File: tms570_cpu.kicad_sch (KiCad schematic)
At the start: 53 parts, among them J12 TSW-103-08-F-S-RA, J3 FTSH-105-01-L-DV-K, U2 TMS570LS0914APGEQQ1

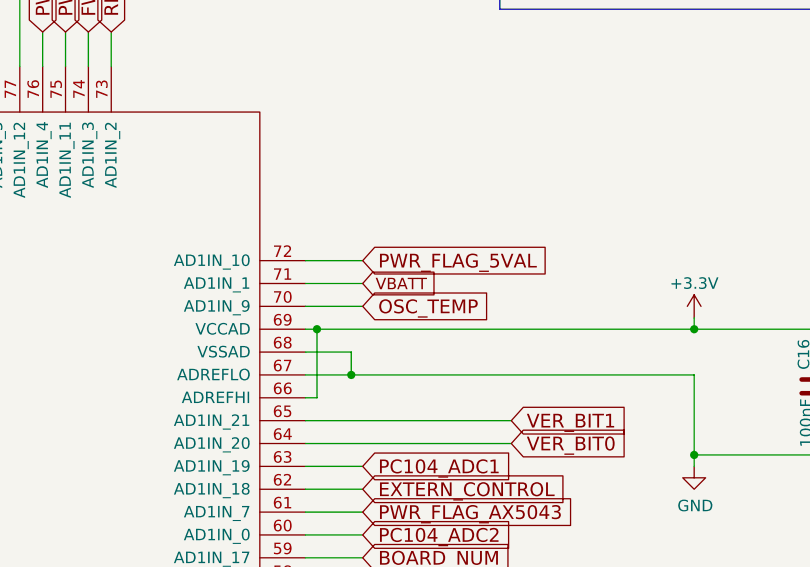
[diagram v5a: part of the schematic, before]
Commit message: Run some more GPIOs from the antenna controller to the PC104
Just for good measure.  Also rename VBATT to VBAT to match the power
supply name.

Signed-off-by: Corey Minyard <corey@minyard.net>
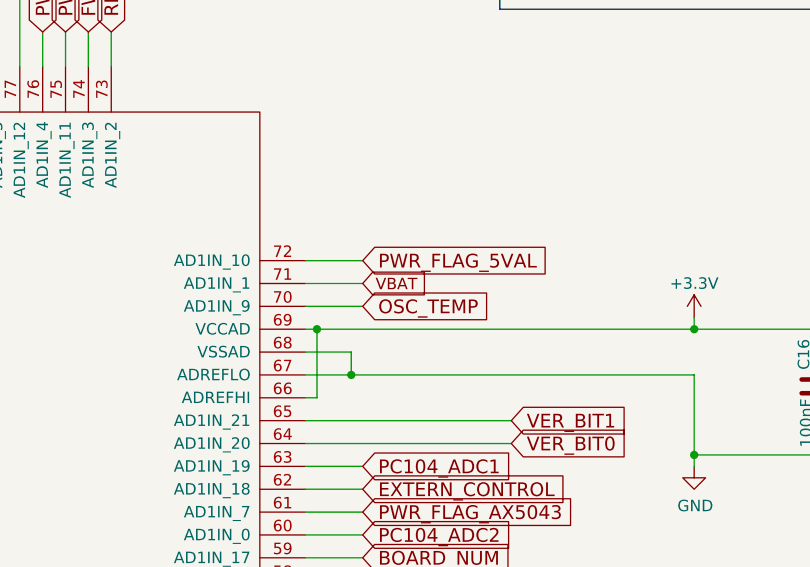
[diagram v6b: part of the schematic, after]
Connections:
- net VBATT renamed VBAT
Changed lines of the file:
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@@
 		)
 	)
-	(global_label "VBATT"
+	(global_label "VBAT"
 		(shape input)
 		(at 288.29 96.52 0)

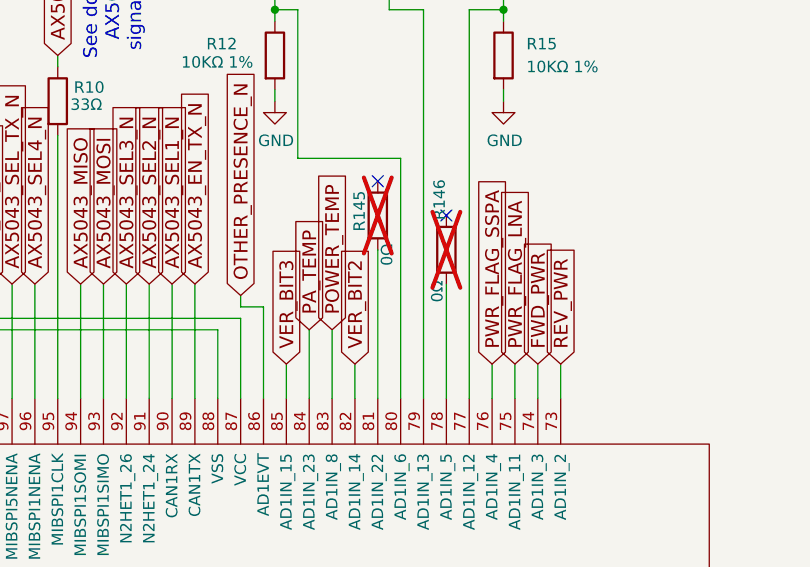
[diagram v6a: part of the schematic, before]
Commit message: Do some work on PC104 ADC/GPIO
Run the last two ADC lines from the TMS570 to the PC104.  Document this
and document how the PC104 lines from the antenna controller may be
used.

Signed-off-by: Corey Minyard <corey@minyard.net>
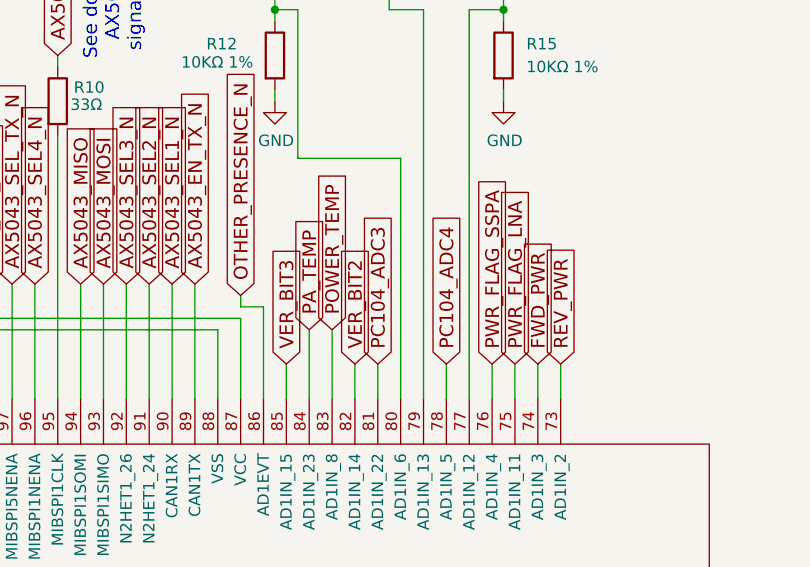
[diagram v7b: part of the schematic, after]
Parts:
- removed R145, R146: 0Ω, Resistor_SMD:R_0402_1005Metric_Pad0.72x0.64mm_HandSolder, symbol Device:R
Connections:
- net PC104_ADC4: now reaches U2.78 (AD1IN_5)
- net PC104_ADC3: now reaches U2.81 (AD1IN_22)
- no-connect marks 4 -> 2
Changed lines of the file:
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@@
 	)
 	(no_connect
-		(at 247.65 52.07)
-	)
-	(no_connect
 		(at 217.17 204.47)
 	)
-	(no_connect
-		(at 240.03 48.26)
-	)
 	(wire
 		(pts
@@
 	(wire
 		(pts
-			(xy 247.65 59.69) (xy 247.65 72.39)
+			(xy 247.65 68.58) (xy 247.65 72.39)
 		)
 		(stroke
@@
 	(wire
 		(pts
-			(xy 240.03 55.88) (xy 240.03 72.39)
+			(xy 240.03 68.58) (xy 240.03 72.39)
 		)
 		(stroke
@@
 		)
 	)
+	(global_label "PC104_ADC3"
+		(shape input)
+		(at 240.03 68.58 90)
+		(fields_autoplaced yes)
+		(effects
+			(font
+				(size 1.524 1.524)
+			)
+			(justify left)
+		)
+		(property "Intersheetrefs" "${INTERSHEET_REFS}"
+			(at 240.03 51.4142 90)
+			(effects
+				(font
+					(size 1.27 1.27)
+				)
+				(justify left)
+				(hide yes)
+			)
+		)
+	)
 	(global_label "OTHER_ACTIVE"
 		(shape input)
@@
 		)
 	)
+	(global_label "PC104_ADC4"
+		(shape input)
+		(at 247.65 68.58 90)
+		(fields_autoplaced yes)
+		(effects
+			(font
+				(size 1.524 1.524)
+			)
+			(justify left)
+		)
+		(property "Intersheetrefs" "${INTERSHEET_REFS}"
+			(at 247.65 51.4142 90)
+			(effects
+				(font
+					(size 1.27 1.27)
+				)
+				(justify left)
+				(hide yes)
+			)
+		)
+	)
 	(global_label "ANT_EN_N"
 		(shape input)
@@
 					(unit 1)
 				)
-			)
-		)
-	)
-	(symbol
-		(lib_id "Device:R")
-		(at 240.03 52.07 0)
-		(unit 1)
-		(exclude_from_sim no)
-		(in_bom no)
-		(on_board yes)
-		(dnp yes)
-		(property "Reference" "R145"
-			(at 237.998 53.848 90)
-			(effects
-				(font
-					(size 1.27 1.27)
-				)
-				(justify left)
-			)
-		)
-		(property "Value" "0Ω"
-			(at 241.046 57.658 90)
-			(effects
-				(font
-					(size 1.27 1.27)
-				)
-				(justify left)
-			)
-		)
-		(property "Footprint" "Resistor_SMD:R_0402_1005Metric_Pad0.72x0.64mm_HandSolder"
-			(at 238.252 52.07 90)
-			(effects
-				(font
-					(size 1.27 1.27)
-				)
-				(hide yes)
-			)
-		)
-		(property "Datasheet" "~"
-			(at 240.03 52.07 0)
-			(effects
-				(font
-					(size 1.27 1.27)
-				)
-				(hide yes)
-			)
-		)
-		(property "Description" ""
-			(at 240.03 52.07 0)
-			(effects
-				(font
-					(size 1.27 1.27)
-				)
-			)
-		)
-		(pin "1"
-		)
-		(pin "2"
-		)
-		(instances
-			(project "PacSat_AFSK"
-				(path "/cc9f42d2-6985-41ac-acab-5ab7b01c5b38/adf61ae3-df77-4e04-8bda-b4049a36fcf4"
-					(reference "R145")
-					(unit 1)
-				)
-			)
-		)
-	)
-	(symbol
-		(lib_id "Device:R")
-		(at 247.65 55.88 0)
-		(unit 1)
-		(exclude_from_sim no)
-		(in_bom no)
-		(on_board yes)
-		(dnp yes)
-		(property "Reference" "R146"
-			(at 246.888 52.578 90)
-			(effects
-				(font
-					(size 1.27 1.27)
-				)
-				(justify left)
-			)
-		)
-		(property "Value" "0Ω"
-			(at 246.634 61.722 90)
-			(effects
-				(font
-					(size 1.27 1.27)
-				)
-				(justify left)
-			)
-		)
-		(property "Footprint" "Resistor_SMD:R_0402_1005Metric_Pad0.72x0.64mm_HandSolder"
-			(at 245.872 55.88 90)
-			(effects
-				(font
-					(size 1.27 1.27)
-				)
-				(hide yes)
-			)
-		)
-		(property "Datasheet" "~"
-			(at 247.65 55.88 0)
-			(effects
-				(font
-					(size 1.27 1.27)
-				)
-				(hide yes)
-			)
-		)
-		(property "Description" ""
-			(at 247.65 55.88 0)
-			(effects
-				(font
-					(size 1.27 1.27)
-				)
-			)
-		)
-		(pin "1"
-		)
-		(pin "2"
-		)
-		(instances
-			(project "PacSat_AFSK"
-				(path "/cc9f42d2-6985-41ac-acab-5ab7b01c5b38/adf61ae3-df77-4e04-8bda-b4049a36fcf4"
-					(reference "R146")
-					(unit 1)
-				)

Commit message: Change board version to 3
Getting ready to release.

Signed-off-by: Corey Minyard <corey@minyard.net>
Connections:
- net +3.3V: now also R22.1
- net GND: no longer R22.1
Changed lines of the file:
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@@
 		)
 	)
-	(text "0"
+	(text "1"
 		(exclude_from_sim no)
 		(at 325.12 30.48 0)
@@
 	)
 	(junction
+		(at 325.12 62.23)
+		(diameter 0)
+		(color 0 0 0 0)
+	)
+	(junction
 		(at 152.4 218.44)
 		(diameter 0)
@@
 	(junction
 		(at 140.97 129.54)
-		(diameter 0)
-		(color 0 0 0 0)
-	)
-	(junction
-		(at 317.5 59.69)
 		(diameter 0)
 		(color 0 0 0 0)
@@
 	(wire
 		(pts
-			(xy 317.5 59.69) (xy 325.12 59.69)
-		)
-		(stroke
-			(width 0)
-			(type default)
-		)
-	)
-	(wire
-		(pts
 			(xy 325.12 115.57) (xy 339.09 115.57)
 		)
@@
 	(wire
 		(pts
-			(xy 325.12 59.69) (xy 325.12 57.15)
-		)
-		(stroke
-			(width 0)
-			(type default)
-		)
-	)
-	(wire
-		(pts
 			(xy 171.45 72.39) (xy 171.45 62.23)
 		)
@@
 	(wire
 		(pts
-			(xy 321.31 62.23) (xy 334.01 62.23)
+			(xy 321.31 62.23) (xy 325.12 62.23)
 		)
 		(stroke
@@
 	(wire
 		(pts
+			(xy 325.12 62.23) (xy 334.01 62.23)
+		)
+		(stroke
+			(width 0)
+			(type default)
+		)
+	)
+	(wire
+		(pts
 			(xy 186.69 64.77) (xy 222.25 64.77)
 		)
@@
 		)
 		(stroke
+			(width 0)
+			(type default)
+		)
+	)
+	(wire
+		(pts
+			(xy 325.12 57.15) (xy 325.12 62.23)
+		)
+		(stroke
